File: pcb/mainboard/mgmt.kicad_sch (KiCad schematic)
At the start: 95 parts, among them J10 FAN_01, J11 XILINX_JTAG, J12 JUMPER_0402_SPDT, J13 JUMPER_0402_SPDT, J14 RJ45, J15 PMOD_HOST, J48 CONN_01X10, J8 FAN_01, J9 CONN_01X03, U23 STM32H735-UFBGA176-25, U24 AT24MAC402, U25 ADM3101E_QFN, U31 ECS-1612MV-250-CN, U32 S25FL128SAGBHIA10, U8 XC7K70T-2FBG484C

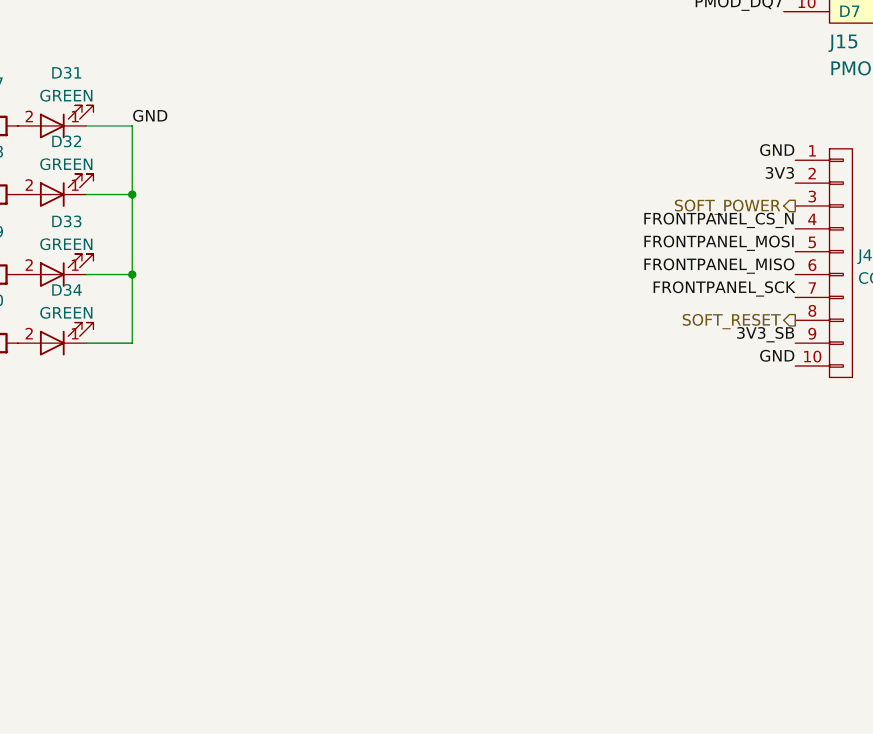
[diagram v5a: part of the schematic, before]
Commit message: Finished initial schematic review of trigger crossbar mainboard
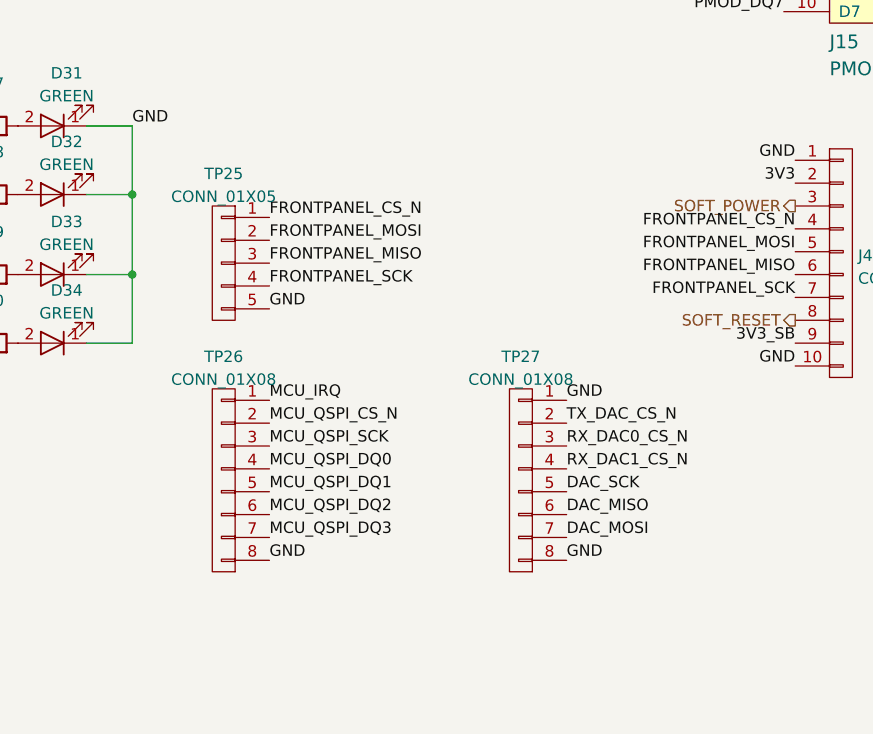
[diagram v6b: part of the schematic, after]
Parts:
- added TP25: CONN_01X05, azonenberg_pcb:CONN_HEADER_2.54MM_1x5, symbol conn:CONN_01X05
- added TP26, TP27: CONN_01X08, azonenberg_pcb:CONN_HEADER_2.54MM_1x8, symbol conn:CONN_01X08
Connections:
- net DAC_MISO: now also TP27.6 (P6)
- net DAC_MOSI: now also TP27.7 (P7)
- net DAC_SCK: now also TP27.5 (P5)
- net FRONTPANEL_CS_N: now also TP25.1 (P1)
- net FRONTPANEL_MISO: now also TP25.3 (P3)
- net FRONTPANEL_MOSI: now also TP25.2 (P2)
- net FRONTPANEL_SCK: now also TP25.4 (P4)
- net GND: now also TP25.5 (P5), TP26.8 (P8), TP27.1 (P1), TP27.8 (P8)
- net MCU_IRQ: now also TP26.1 (P1)
- net MCU_QSPI_CS_N: now also TP26.2 (P2)
- net MCU_QSPI_DQ0: now also TP26.4 (P4)
- net MCU_QSPI_DQ1: now also TP26.5 (P5)
- net MCU_QSPI_DQ2: now also TP26.6 (P6)
- net MCU_QSPI_DQ3: now also TP26.7 (P7)
- net MCU_QSPI_SCK: now also TP26.3 (P3)
- net RX_DAC0_CS_N: now also TP27.3 (P3)
- net RX_DAC1_CS_N: now also TP27.4 (P4)
- net TX_DAC_CS_N: now also TP27.2 (P2)
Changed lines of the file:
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@@
   (title_block
     (title "Trigger Crossbar")
-    (date "2023-12-18")
+    (date "2023-12-19")
     (rev "0.1")
     (company "Antikernel Labs")
@@
   (no_connect (at 245.11 81.28))
   (no_connect (at 354.33 91.44))
-  (no_connect (at 354.33 76.2))
   (no_connect (at 280.67 50.8))
   (no_connect (at 152.4 55.88))
@@
   (no_connect (at 287.02 99.06))
   (no_connect (at 280.67 38.1))
-  (no_connect (at 354.33 78.74))
   (no_connect (at 245.11 40.64))
   (no_connect (at 245.11 99.06))
@@
   (no_connect (at 280.67 53.34))
   (no_connect (at 280.67 33.02))
+  (no_connect (at 354.33 76.2))
   (no_connect (at 287.02 116.84))
   (no_connect (at 354.33 99.06))
@@
   (no_connect (at 354.33 50.8))
   (no_connect (at 245.11 96.52))
+  (no_connect (at 354.33 78.74))
   (no_connect (at 245.11 66.04))
   (no_connect (at 245.11 50.8))
@@
     (effects (font (size 1.27 1.27)) (justify right bottom))
   )
+  (label "DAC_MOSI" (at 358.14 246.38 0)
+    (effects (font (size 1.27 1.27)) (justify left bottom))
+  )
   (label "RS232_RX" (at 214.63 240.03 180)
     (effects (font (size 1.27 1.27)) (justify right bottom))
@@
     (effects (font (size 1.27 1.27)) (justify right bottom))
   )
+  (label "GND" (at 358.14 248.92 0)
+    (effects (font (size 1.27 1.27)) (justify left bottom))
+  )
   (label "FRONTPANEL_MOSI" (at 383.54 214.63 180)
     (effects (font (size 1.27 1.27)) (justify right bottom))
@@
     (effects (font (size 1.27 1.27)) (justify right bottom))
   )
+  (label "DAC_MISO" (at 358.14 243.84 0)
+    (effects (font (size 1.27 1.27)) (justify left bottom))
+  )
   (label "FAN2_TACH" (at 87.63 223.52 180)
     (effects (font (size 1.27 1.27)) (justify right bottom))
@@
     (effects (font (size 1.27 1.27)) (justify right bottom))
   )
+  (label "GND" (at 325.12 248.92 0)
+    (effects (font (size 1.27 1.27)) (justify left bottom))
+  )
   (label "RS232_TX" (at 214.63 245.11 180)
     (effects (font (size 1.27 1.27)) (justify right bottom))
@@
     (effects (font (size 1.27 1.27)) (justify right bottom))
   )
+  (label "MCU_QSPI_DQ1" (at 325.12 241.3 0)
+    (effects (font (size 1.27 1.27)) (justify left bottom))
+  )
   (label "MCU_LED3" (at 138.43 271.78 180)
     (effects (font (size 1.27 1.27)) (justify right bottom))
@@
     (effects (font (size 1.27 1.27)) (justify right bottom))
   )
+  (label "MCU_QSPI_DQ2" (at 325.12 243.84 0)
+    (effects (font (size 1.27 1.27)) (justify left bottom))
+  )
+  (label "MCU_IRQ" (at 325.12 231.14 0)
+    (effects (font (size 1.27 1.27)) (justify left bottom))
+  )
   (label "MCU_QSPI_CS_N" (at 354.33 124.46 180)
     (effects (font (size 1.27 1.27)) (justify right bottom))
@@
     (effects (font (size 1.27 1.27)) (justify right bottom))
   )
+  (label "MCU_QSPI_SCK" (at 325.12 236.22 0)
+    (effects (font (size 1.27 1.27)) (justify left bottom))
+  )
   (label "3V3" (at 142.24 135.89 180)
     (effects (font (size 1.27 1.27)) (justify right bottom))
@@
     (effects (font (size 1.27 1.27)) (justify right bottom))
   )
+  (label "GND" (at 325.12 220.98 0)
+    (effects (font (size 1.27 1.27)) (justify left bottom))
+  )
   (label "MCU_QSPI_DQ0" (at 354.33 119.38 180)
     (effects (font (size 1.27 1.27)) (justify right bottom))
@@
     (effects (font (size 1.27 1.27)) (justify right bottom))
   )
+  (label "FRONTPANEL_SCK" (at 325.12 218.44 0)
+    (effects (font (size 1.27 1.27)) (justify left bottom))
+  )
   (label "I2C_SCL" (at 171.45 165.1 0)
     (effects (font (size 1.27 1.27)) (justify left bottom))
@@
     (effects (font (size 1.27 1.27)) (justify left bottom))
   )
+  (label "FRONTPANEL_MOSI" (at 325.12 213.36 0)
+    (effects (font (size 1.27 1.27)) (justify left bottom))
+  )
   (label "PMOD_DQ5" (at 382.27 182.88 180)
     (effects (font (size 1.27 1.27)) (justify right bottom))
   )
+  (label "DAC_SCK" (at 358.14 241.3 0)
+    (effects (font (size 1.27 1.27)) (justify left bottom))
+  )
   (label "3V3" (at 30.48 213.36 180)
     (effects (font (size 1.27 1.27)) (justify right bottom))
@@
     (effects (font (size 1.27 1.27)) (justify left bottom))
   )
+  (label "MCU_QSPI_DQ3" (at 325.12 246.38 0)
+    (effects (font (size 1.27 1.27)) (justify left bottom))
+  )
   (label "MCU_QSPI_DQ2" (at 245.11 33.02 180)
     (effects (font (size 1.27 1.27)) (justify right bottom))
@@
     (effects (font (size 1.27 1.27)) (justify left bottom))
   )
+  (label "MCU_QSPI_CS_N" (at 325.12 233.68 0)
+    (effects (font (size 1.27 1.27)) (justify left bottom))
+  )
   (label "FLASH_CS_N" (at 284.48 167.64 180)
     (effects (font (size 1.27 1.27)) (justify right bottom))
@@
     (effects (font (size 1.27 1.27)) (justify right bottom))
   )
+  (label "FRONTPANEL_MISO" (at 325.12 215.9 0)
+    (effects (font (size 1.27 1.27)) (justify left bottom))
+  )
   (label "FLASH_DQ3" (at 332.74 165.1 0)
     (effects (font (size 1.27 1.27)) (justify left bottom))
@@
     (effects (font (size 1.27 1.27)) (justify right bottom))
   )
+  (label "RX_DAC0_CS_N" (at 358.14 236.22 0)
+    (effects (font (size 1.27 1.27)) (justify left bottom))
+  )
   (label "PMOD_DQ7" (at 354.33 144.78 180)
     (effects (font (size 1.27 1.27)) (justify right bottom))
@@
     (effects (font (size 1.27 1.27)) (justify right bottom))
   )
+  (label "FRONTPANEL_CS_N" (at 325.12 210.82 0)
+    (effects (font (size 1.27 1.27)) (justify left bottom))
+  )
   (label "I2C_SDA" (at 171.45 167.64 0)
     (effects (font (size 1.27 1.27)) (justify left bottom))
@@
     (effects (font (size 1.27 1.27)) (justify right bottom))
   )
+  (label "TX_DAC_CS_N" (at 358.14 233.68 0)
+    (effects (font (size 1.27 1.27)) (justify left bottom))
+  )
   (label "GND" (at 29.21 175.26 180)
     (effects (font (size 1.27 1.27)) (justify right bottom))
@@
     (effects (font (size 1.27 1.27)) (justify right bottom))
   )
+  (label "RX_DAC1_CS_N" (at 358.14 238.76 0)
+    (effects (font (size 1.27 1.27)) (justify left bottom))
+  )
   (label "MCU_RST_N" (at 40.64 196.85 180)
     (effects (font (size 1.27 1.27)) (justify right bottom))
@@
     (effects (font (size 1.27 1.27)) (justify right bottom))
   )
+  (label "MCU_QSPI_DQ0" (at 325.12 238.76 0)
+    (effects (font (size 1.27 1.27)) (justify left bottom))
+  )
   (label "3V3" (at 171.45 172.72 0)
     (effects (font (size 1.27 1.27)) (justify left bottom))
@@
     (effects (font (size 1.27 1.27)) (justify left bottom))
   )
+  (label "GND" (at 358.14 231.14 0)
+    (effects (font (size 1.27 1.27)) (justify left bottom))
+  )
   (label "3V3" (at 142.24 148.59 180)
     (effects (font (size 1.27 1.27)) (justify right bottom))
@@
     (pin "4")
   )
+  (symbol (lib_id "conn:CONN_01X08") (at 320.04 240.03 0) (mirror y) (unit 1)
+    (in_bom yes) (on_board yes) (fields_autoplaced)
+    (property "Reference" "TP26" (id 0) (at 320.04 226.2972 0))
+    (property "Value" "CONN_01X08" (id 1) (at 320.04 228.8341 0))
+    (property "Footprint" "azonenberg_pcb:CONN_HEADER_2.54MM_1x8" (id 2) (at 320.04 240.03 0)
+      (effects (font (size 1.27 1.27)) hide)
+    )
+    (property "Datasheet" "" (id 3) (at 320.04 240.03 0)
+      (effects (font (size 1.27 1.27)) hide)
+    )
+    (pin "1")
+    (pin "2")
+    (pin "3")
+    (pin "4")
+    (pin "5")
+    (pin "6")
+    (pin "7")
+    (pin "8")
+  )
   (symbol (lib_id "device:C") (at 124.46 204.47 0) (unit 1)
     (in_bom yes) (on_board yes) (fields_autoplaced)
@@
     (pin "2")
   )
+  (symbol (lib_id "conn:CONN_01X08") (at 353.06 240.03 0) (mirror y) (unit 1)
+    (in_bom yes) (on_board yes) (fields_autoplaced)
+    (property "Reference" "TP27" (id 0) (at 353.06 226.2972 0))
+    (property "Value" "CONN_01X08" (id 1) (at 353.06 228.8341 0))
+    (property "Footprint" "azonenberg_pcb:CONN_HEADER_2.54MM_1x8" (id 2) (at 353.06 240.03 0)
+      (effects (font (size 1.27 1.27)) hide)
+    )
+    (property "Datasheet" "" (id 3) (at 353.06 240.03 0)
+      (effects (font (size 1.27 1.27)) hide)
+    )
+    (pin "1")
+    (pin "2")
+    (pin "3")
+    (pin "4")
+    (pin "5")
+    (pin "6")
+    (pin "7")
+    (pin "8")
+  )
   (symbol (lib_id "device:R") (at 325.12 160.02 90) (unit 1)
     (in_bom yes) (on_board yes)
@@
     (pin "2")
   )
+  (symbol (lib_id "conn:CONN_01X05") (at 320.04 215.9 0) (mirror y) (unit 1)
+    (in_bom yes) (on_board yes) (fields_autoplaced)
+    (property "Reference" "TP25" (id 0) (at 320.04 205.9772 0))
+    (property "Value" "CONN_01X05" (id 1) (at 320.04 208.5141 0))
+    (property "Footprint" "azonenberg_pcb:CONN_HEADER_2.54MM_1x5" (id 2) (at 320.04 215.9 0)
+      (effects (font (size 1.27 1.27)) hide)
+    )
+    (property "Datasheet" "" (id 3) (at 320.04 215.9 0)
+      (effects (font (size 1.27 1.27)) hide)
+    )
+    (pin "1")
+    (pin "2")
+    (pin "3")
+    (pin "4")
+    (pin "5")
+  )
   (symbol (lib_id "device:R") (at 346.71 27.94 90) (unit 1)
